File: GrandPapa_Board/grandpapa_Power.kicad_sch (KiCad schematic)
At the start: 32 parts, among them U1 LT1576IS8-5#TRPBF, U11 INA180, U2 TPS61023DRLT, U5 FPF2124

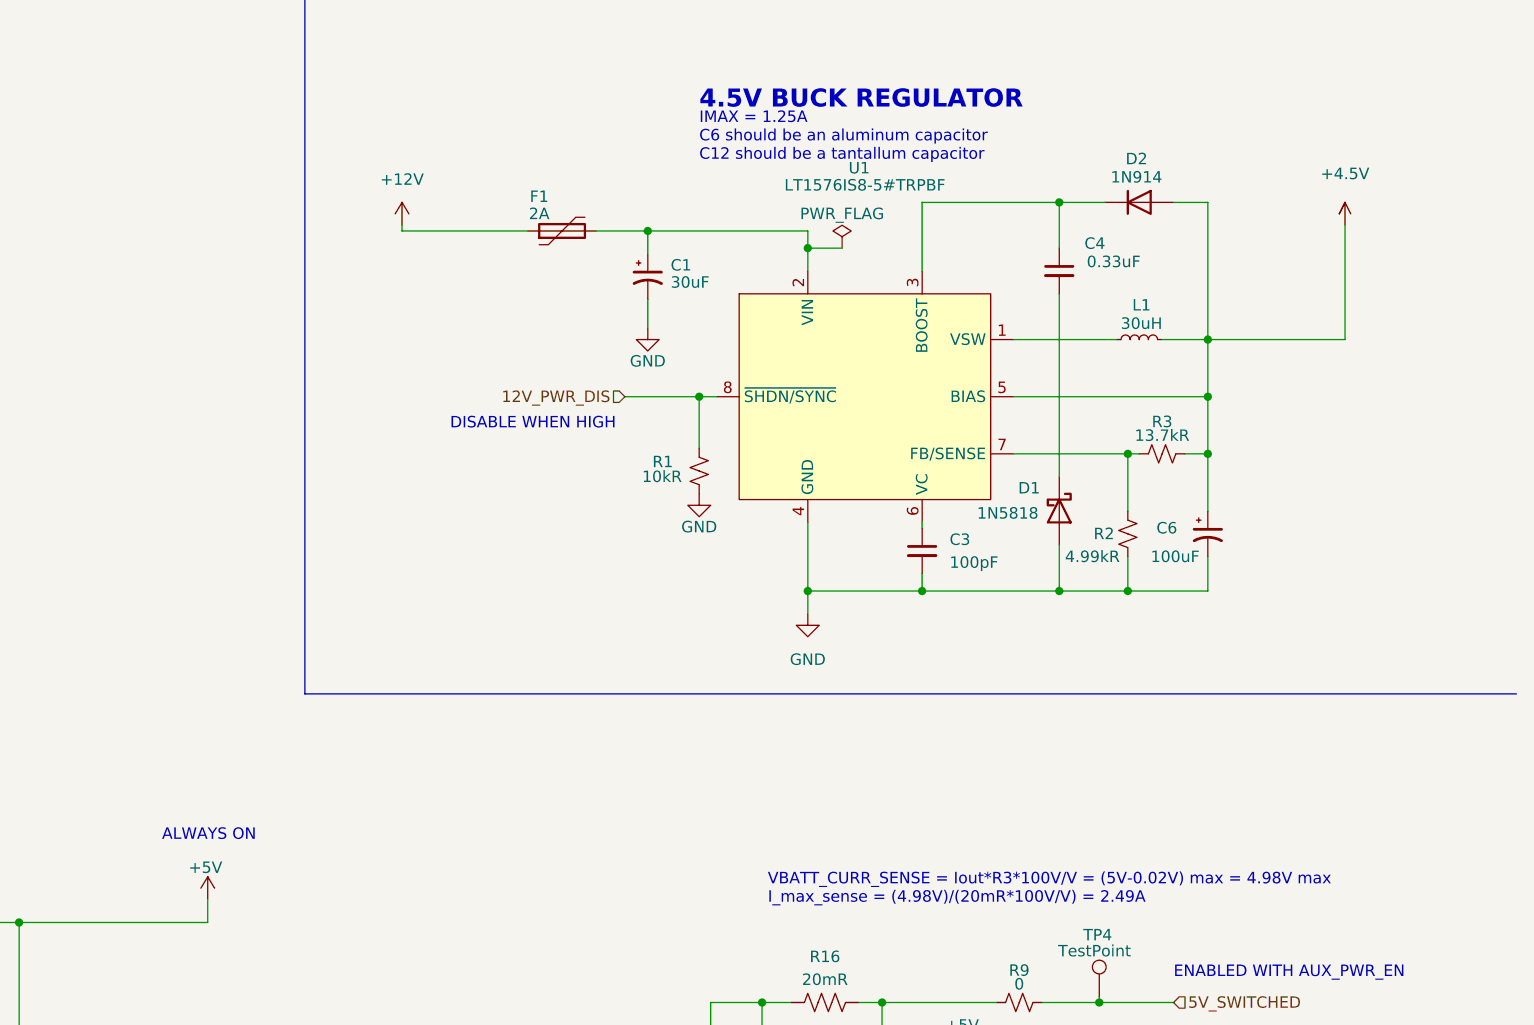
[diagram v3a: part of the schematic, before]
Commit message: fix SHDN pin config on 4.5V regulator
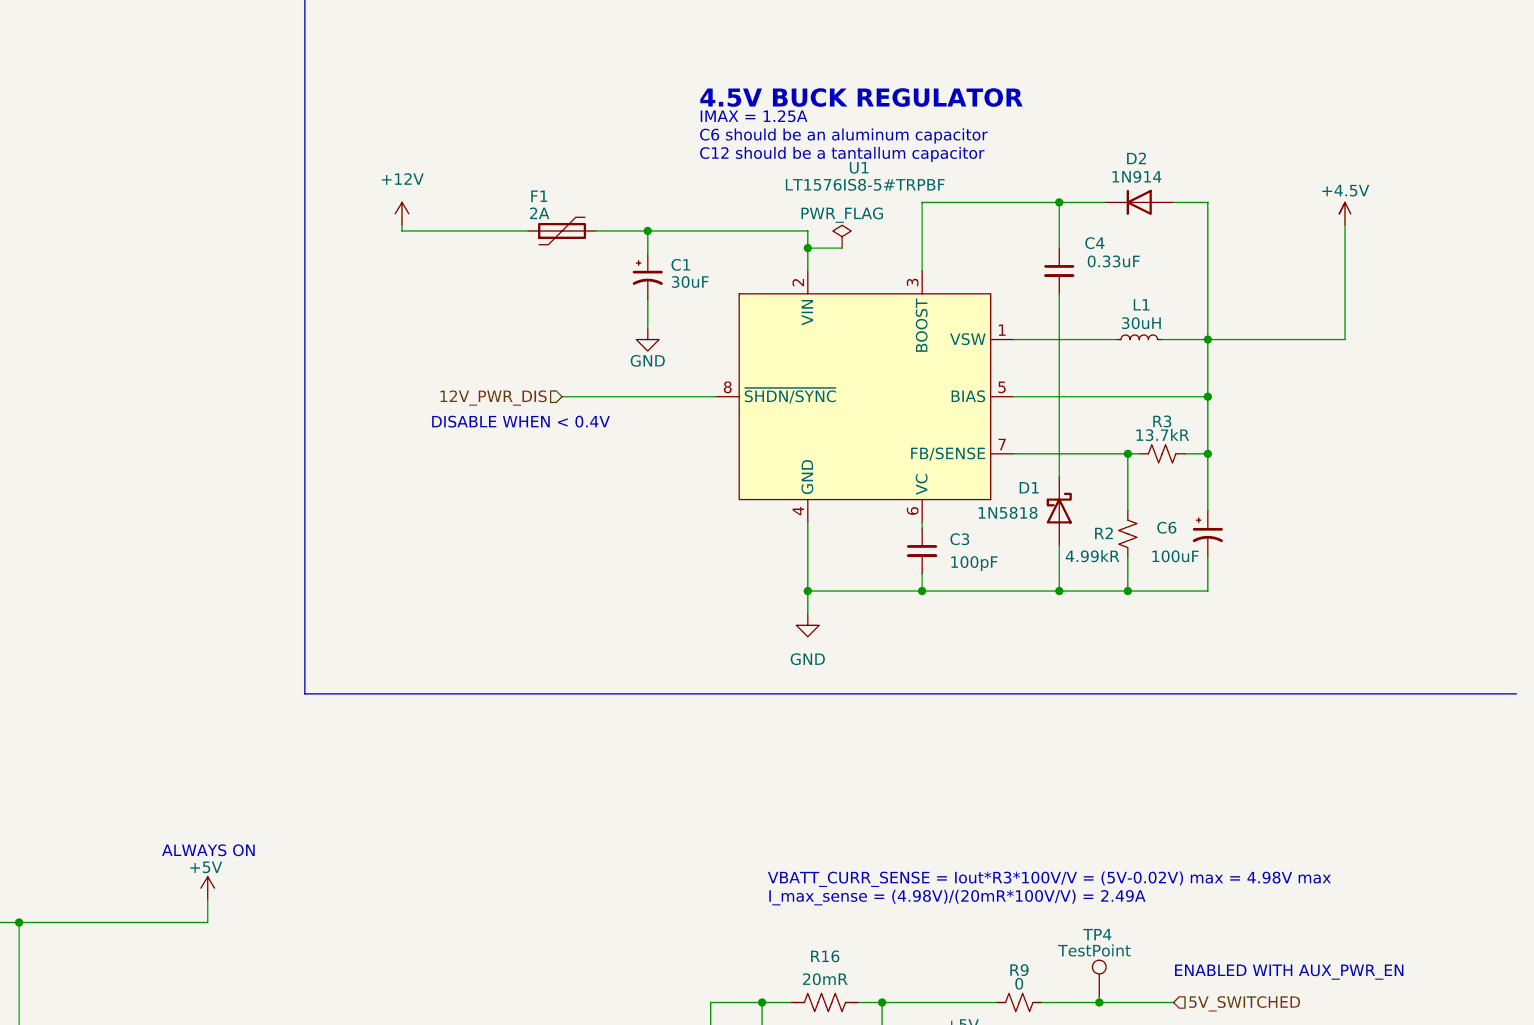
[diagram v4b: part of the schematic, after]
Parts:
- removed R1: 10kR, symbol Device:R_Small_US
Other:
- note added: "DISABLE WHEN < 0.4V"
- note removed: "DISABLE WHEN HIGH"
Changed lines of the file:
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@@
   (junction (at 86.995 114.3) (diameter 0) (color 0 0 0 0)
   )
-  (junction (at 194.31 55.88) (diameter 0) (color 0 0 0 0)
-  )
   (junction (at 45.72 109.855) (diameter 0) (color 0 0 0 0)
   )
@@
     (stroke (width 0) (type default) (color 0 0 0 0))
   )
-  (wire (pts (xy 194.31 55.88) (xy 194.31 61.595))
-    (stroke (width 0) (type default) (color 0 0 0 0))
-  )
   (wire (pts (xy 188.595 45.085) (xy 188.595 48.26))
     (stroke (width 0) (type default) (color 0 0 0 0))
@@
     (stroke (width 0) (type default) (color 0 0 0 0))
   )
-  (wire (pts (xy 186.055 55.88) (xy 194.31 55.88))
-    (stroke (width 0) (type default) (color 0 0 0 0))
-  )
   (wire (pts (xy 250.825 62.23) (xy 250.825 68.58))
     (stroke (width 0) (type default) (color 0 0 0 0))
   )
-  (wire (pts (xy 196.215 55.88) (xy 194.31 55.88))
-    (stroke (width 0) (type default) (color 0 0 0 0))
-  )
   (wire (pts (xy 154.94 146.685) (xy 156.845 146.685))
     (stroke (width 0) (type default) (color 0 0 0 0))
@@
   )
   (wire (pts (xy 99.695 114.3) (xy 109.22 114.3))
+    (stroke (width 0) (type default) (color 0 0 0 0))
+  )
+  (wire (pts (xy 179.07 55.88) (xy 196.215 55.88))
     (stroke (width 0) (type default) (color 0 0 0 0))
   )
@@
     (effects (font (size 1.27 1.27)) (justify left bottom))
   )
-  (text "DISABLE WHEN HIGH\n" (at 166.624 59.69 0)
+  (text "DISABLE WHEN < 0.4V\n" (at 164.465 59.69 0)
     (effects (font (size 1.27 1.27)) (justify left bottom))
   )
@@
     (effects (font (size 1.27 1.27)) (justify left bottom))
   )
-  (text "ALWAYS ON" (at 134.62 105.41 0)
+  (text "ALWAYS ON" (at 134.62 107.315 0)
     (effects (font (size 1.27 1.27)) (justify left bottom))
   )
@@
     (effects (font (size 1.27 1.27)) (justify left bottom))
   )
-  (hierarchical_label "12V_PWR_DIS" (shape input) (at 186.055 55.88 180)
+  (hierarchical_label "12V_PWR_DIS" (shape input) (at 179.07 55.88 180)
     (effects (font (size 1.27 1.27)) (justify right))
   )
@@
   (hierarchical_label "AUX_CURR_SENSE" (shape input) (at 243.84 147.32 0)
     (effects (font (size 1.27 1.27)) (justify left))
-  )
-  (symbol (lib_id "power:GND") (at 194.31 66.675 0) (unit 1)
-    (in_bom yes) (on_board yes)
-    (property "Reference" "#PWR011" (id 0) (at 194.31 73.025 0)
-      (effects (font (size 1.27 1.27)) hide)
-    )
-    (property "Value" "GND" (id 1) (at 194.31 70.358 0))
-    (property "Footprint" "" (id 2) (at 194.31 66.675 0)
-      (effects (font (size 1.27 1.27)) hide)
-    )
-    (property "Datasheet" "" (id 3) (at 194.31 66.675 0)
-      (effects (font (size 1.27 1.27)) hide)
-    )
-    (pin "1")
   )
   (symbol (lib_id "grandpapa board:FPF2124") (at 164.465 146.685 0) (unit 1)
@@
   )
   (symbol (lib_id "grandpapa board:+4.5V") (at 266.065 34.29 0) (unit 1)
-    (in_bom yes) (on_board yes) (fields_autoplaced)
+    (in_bom yes) (on_board yes)
     (property "Reference" "#PWR013" (id 0) (at 266.065 31.115 0)
       (effects (font (size 1.27 1.27)) hide)
     )
-    (property "Value" "+4.5V" (id 1) (at 266.065 31.115 0))
+    (property "Value" "+4.5V" (id 1) (at 266.065 33.02 0))
     (property "Footprint" "" (id 2) (at 272.415 33.02 0)
       (effects (font (size 1.27 1.27)) hide)
@@
     (pin "1")
   )
-  (symbol (lib_id "Device:R_Small_US") (at 194.31 64.135 0) (unit 1)
-    (in_bom yes) (on_board yes)
-    (property "Reference" "R1" (id 0) (at 189.103 63.119 0)
-      (effects (font (size 1.27 1.27)) (justify left))
-    )
-    (property "Value" "10kR" (id 1) (at 187.96 64.77 0)
-      (effects (font (size 1.27 1.27)) (justify left))
-    )
-    (property "Footprint" "" (id 2) (at 194.31 64.135 0)
-      (effects (font (size 1.27 1.27)) hide)
-    )
-    (property "Datasheet" "~" (id 3) (at 194.31 64.135 0)
-      (effects (font (size 1.27 1.27)) hide)
-    )
-    (pin "1")
-    (pin "2")
-  )
   (symbol (lib_id "Device:C_Small") (at 109.22 117.475 0) (unit 1)

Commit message: Addressed some Jack comments. 3/4/6/7 TBD
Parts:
- removed C20: 0.1uF, Capacitor_SMD:C_0805_2012Metric_Pad1.18x1.45mm_HandSolder, symbol Device:C
- removed R16: 20mR, Resistor_SMD:R_1206_3216Metric_Pad1.30x1.75mm_HandSolder, symbol Device:R_US
- removed R9: 0, symbol Device:R_Small_US
- removed TP4: TestPoint, Connector_PinHeader_2.54mm:PinHeader_1x01_P2.54mm_Vertical, symbol Connector:TestPoint
- removed U11: INA180, symbol CANHW:INA180
- added C?: 0.1uF, Capacitor_SMD:C_0805_2012Metric_Pad1.18x1.45mm_HandSolder, symbol Device:C
- added R?: 20mR, Resistor_SMD:R_1206_3216Metric_Pad1.30x1.75mm_HandSolder, symbol Device:R_US
- added R?: 0, symbol Device:R_Small_US
- added R?: 10kR, Resistor_SMD:R_1206_3216Metric_Pad1.30x1.75mm_HandSolder, symbol Device:R_US
- added TP?: TestPoint, Connector_PinHeader_2.54mm:PinHeader_1x01_P2.54mm_Vertical, symbol Connector:TestPoint
- added U?: INA180, symbol CANHW:INA180
- F2: value 2A -> 1A
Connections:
- net +4.5V: now also R?.1
- net +5V: now also C?.2, U?.5 (VS)
- net 12V_PWR_DIS: now also R?.2
- net 5V_SWITCHED: now also C13.1, U5.5 (VOUT)
- net AUX_CURR_SENSE: now also U?.1 (VO)
- net GND: now also C?.1, U?.2 (GND)
- net at L1.1, U1.1 (VSW): now also C4.2, D1.1 (K)
- net at C1.1, U1.2 (VIN): now also R?.2, TP?.1; no longer F1.2
- new net: F1.2, R?.2, U?.3 (IN+)
- new net: R?.1, R?.1, U?.4 (IN-)
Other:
- note added: "Convoluted Payload Power Path 101 1. 12V supply power is provided from the rocket (only while on the pad prior to flight) 2. U1 regulates the 12V supply down to 4.5V, which is what our battery charger IC can take 3. Our battery charger takes 4.5V in and charges the battery, as well as passing the 4.5V supply onward to supply power to everything else. When it loses that external source, it switche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"
- note added: "IMAX = 1A"
- note removed: "IMAX = 2A"
- moved on the sheet: C1, C13, C2, C3, C4, C5, C6, C7, C8, D1, D2, F1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

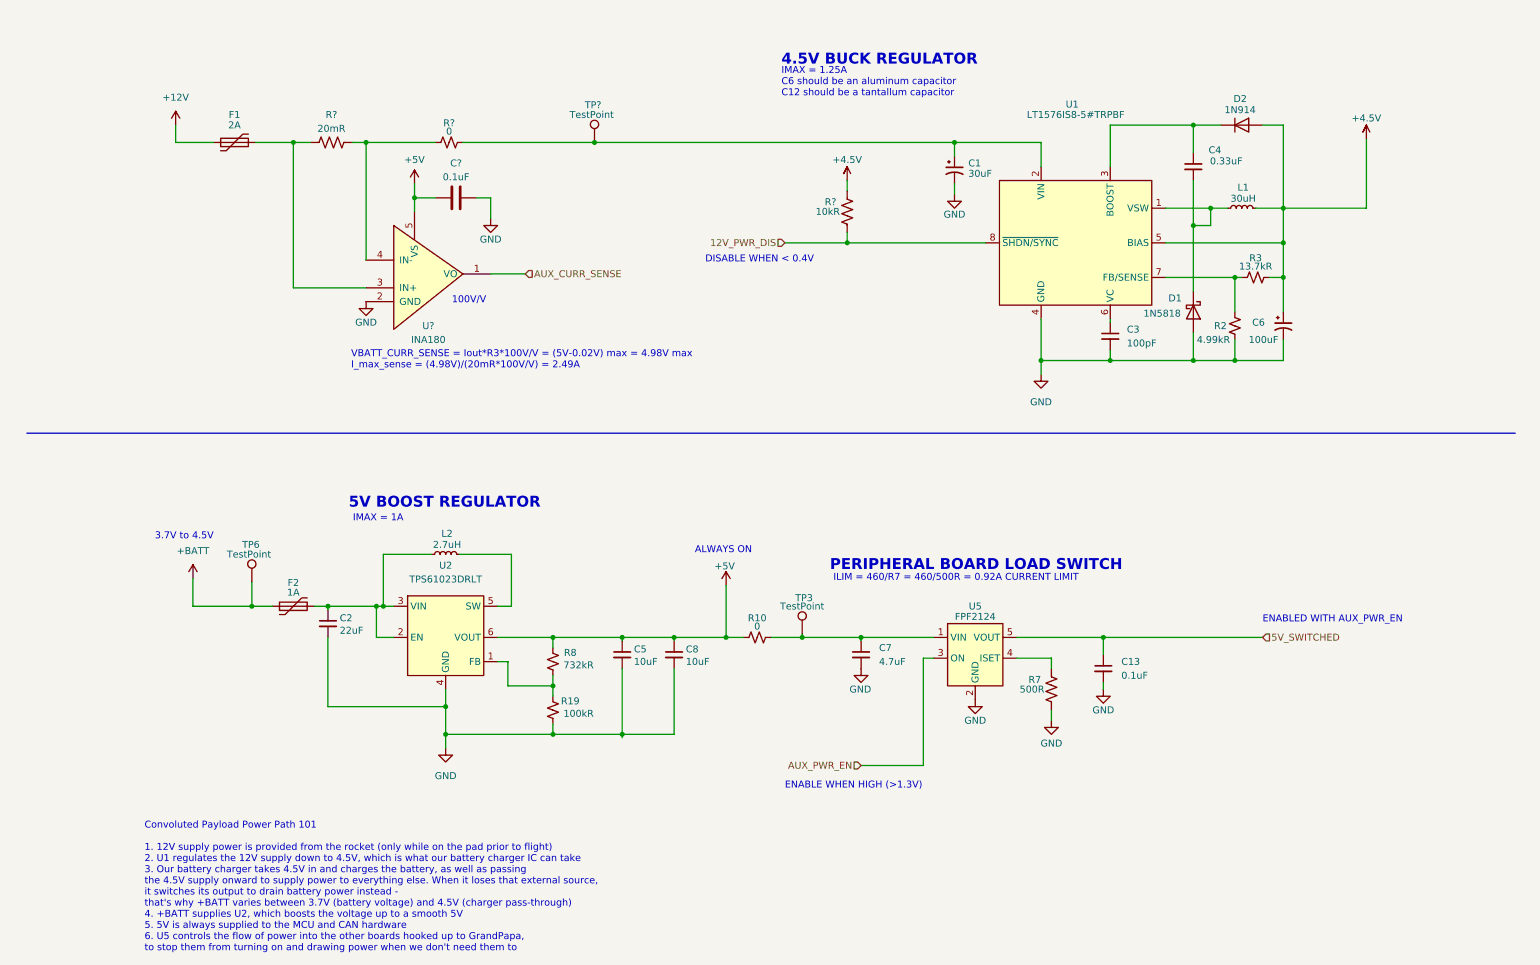
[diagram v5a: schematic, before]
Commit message: address the rest of jack's review, still need to fix grid spacing
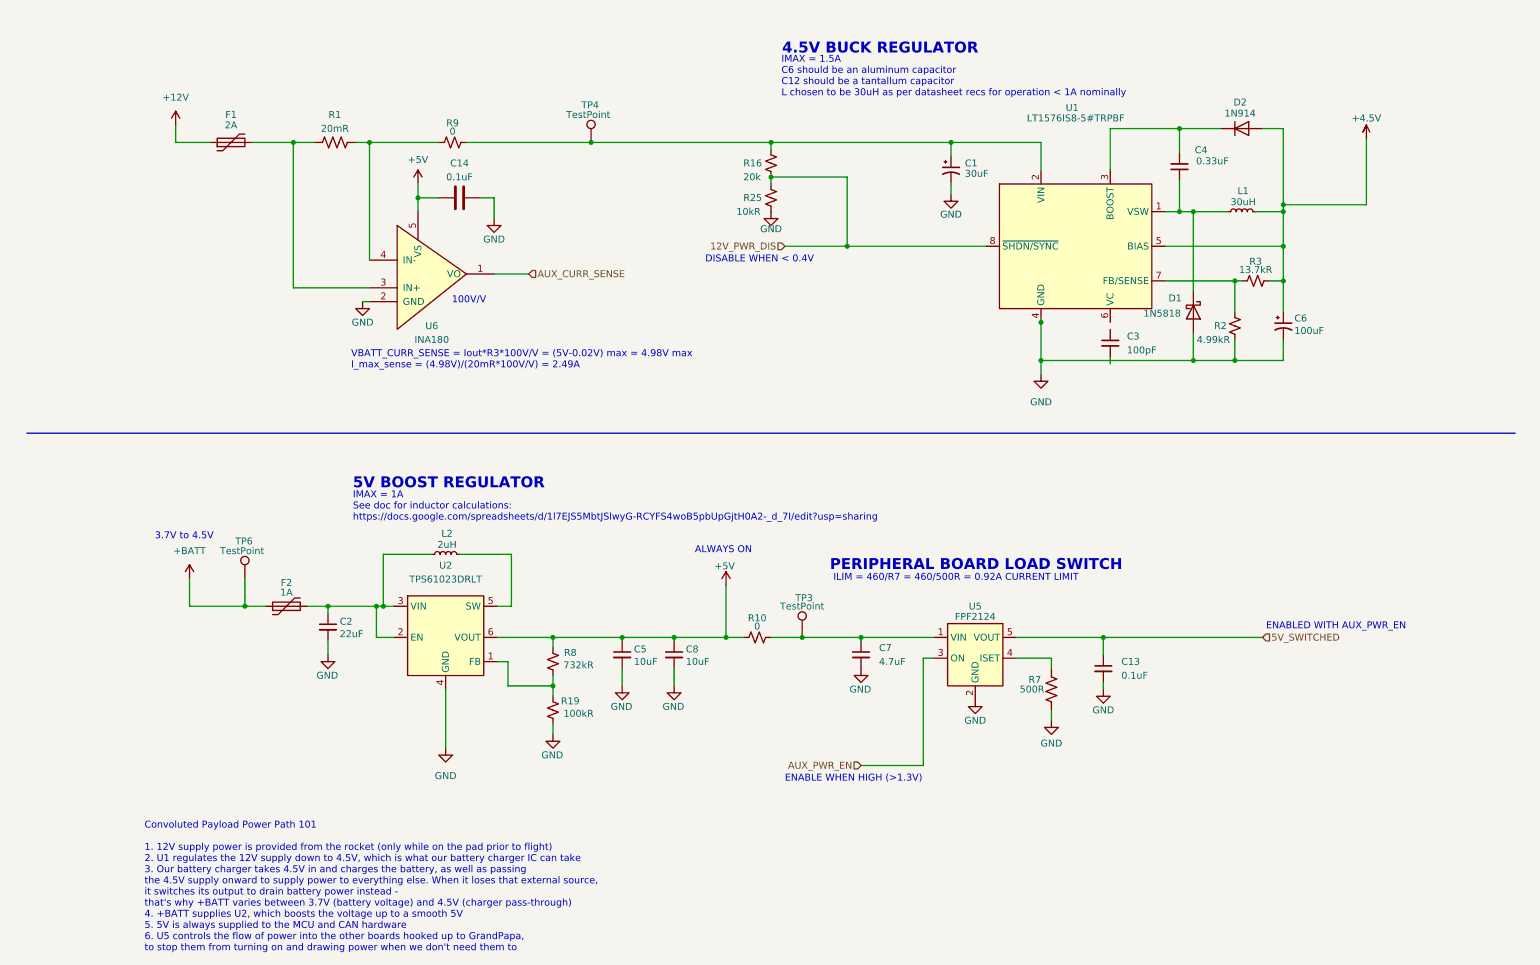
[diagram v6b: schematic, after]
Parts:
- removed R?: 10kR, Resistor_SMD:R_1206_3216Metric_Pad1.30x1.75mm_HandSolder, symbol Device:R_US
- added R16: 20k, symbol Device:R_Small_US
- added R25: 10kR, symbol Device:R_Small_US
- L2: value 2.7uH -> 2uH
- gave numbers to parts that had none: 5
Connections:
- net 12V_PWR_DIS: now also R16.1, R25.2
- net GND: now also R25.1; no longer C3.2
- net at C1.1, R9.2, TP4.1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: now also R16.2
- net at U1.6 (VC): no longer C3.1
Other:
- note added: "IMAX = 1.5A C6 should be an aluminum capacitor C12 should be a tantallum capacitor L chosen to be 30uH as per datasheet recs for operation < 1A nominally"
- note added: "IMAX = 1A See doc for inductor calculations: https://docs.google.com/spreadsheets/d/1l7EJS5MbtJSlwyG-RCYFS4woB5pbUpGjtH0A2-_d_7I/edit?usp=sharing"
- note removed: "IMAX = 1.25A C6 should be an aluminum capacitor C12 should be a tantallum capacitor"
- note removed: "IMAX = 1A"
- moved on the sheet: C1, C14, C2, C3, C4, D2, F1, F2, L1, R1, R3, R9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
